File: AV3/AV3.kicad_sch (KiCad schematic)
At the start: 2 parts, among them U1 LCD-16X2

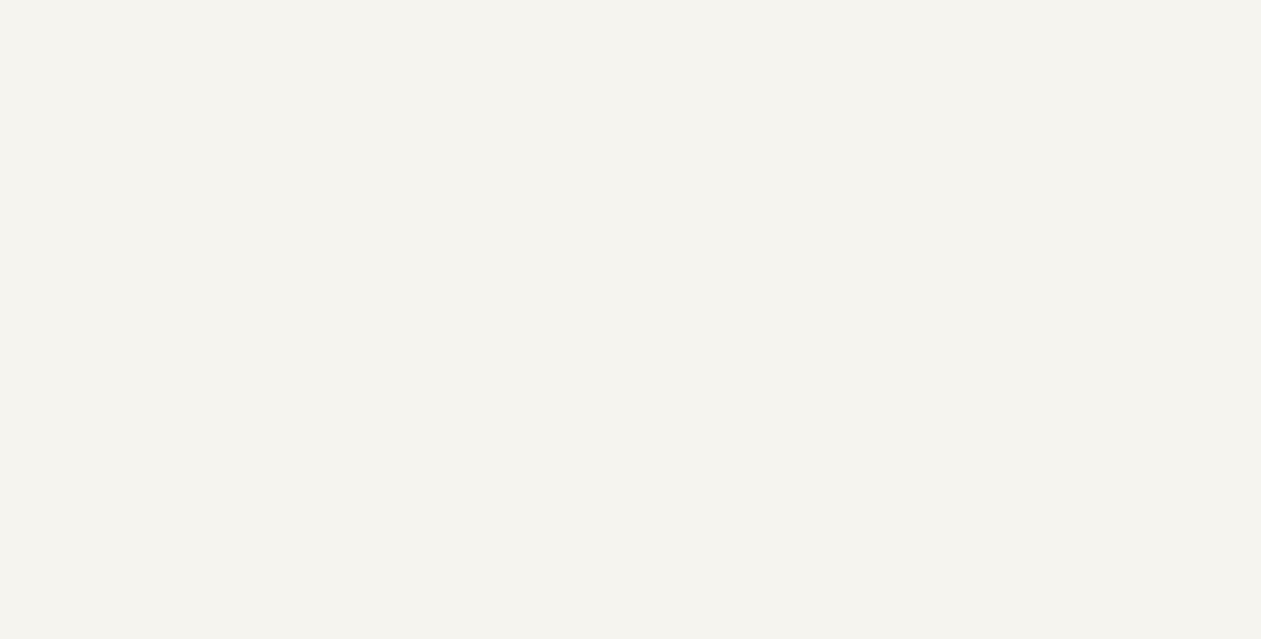
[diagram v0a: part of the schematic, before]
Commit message: Add power supply circuitry
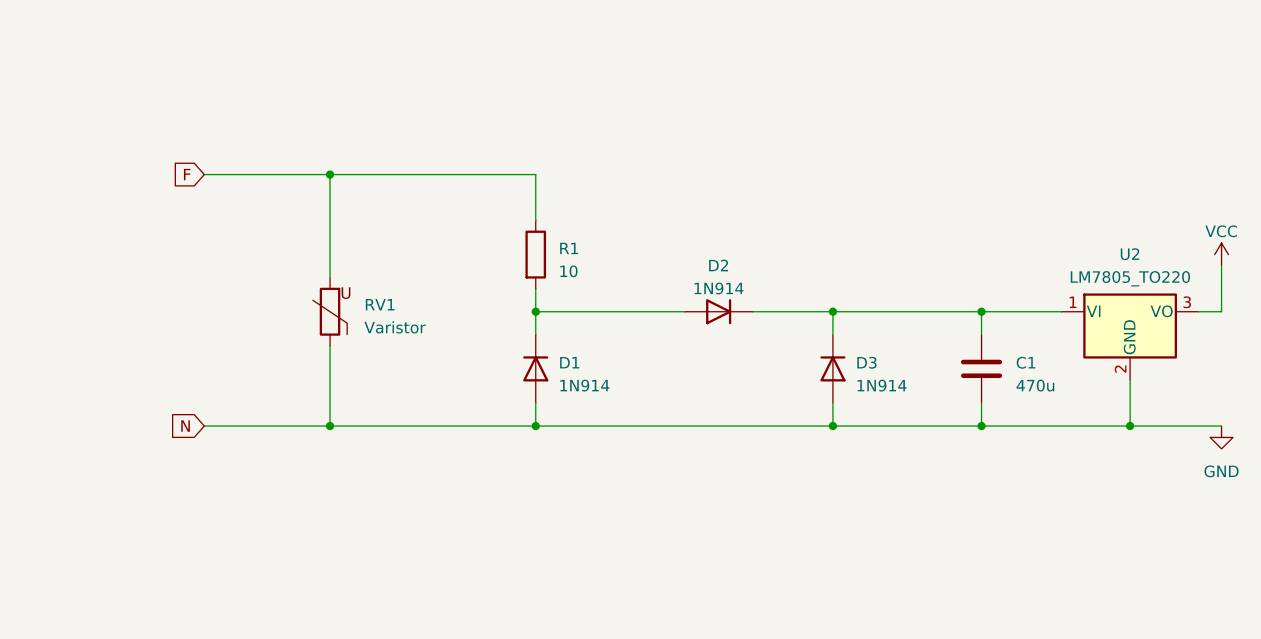
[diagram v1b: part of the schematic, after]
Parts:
- added C1: 470u, Capacitor_THT:CP_Radial_D10.0mm_P2.50mm, symbol Device:C
- added D1, D2, D3: 1N914, Diode_THT:D_DO-35_SOD27_P7.62mm_Horizontal, symbol Diode:1N914
- added R1: 10, Resistor_THT:R_Axial_DIN0204_L3.6mm_D1.6mm_P2.54mm_Vertical, symbol Device:R
- added RV1: Varistor, Varistor:RV_Disc_D7mm_W3.4mm_P5mm, symbol Device:Varistor
- added U2: LM7805_TO220, Package_TO_SOT_THT:TO-220-3_Vertical, symbol Regulator_Linear:LM7805_TO220
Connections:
- net GND: now also C1.2, D1.2 (A), D3.2 (A), RV1.1, U2.2 (GND)
- net VCC: now also U2.3 (VO)
- new net: C1.1, D2.1 (K), D3.1 (K), U2.1 (VI)
- new net: D1.1 (K), D2.2 (A), R1.2
- new net F: R1.1, RV1.2

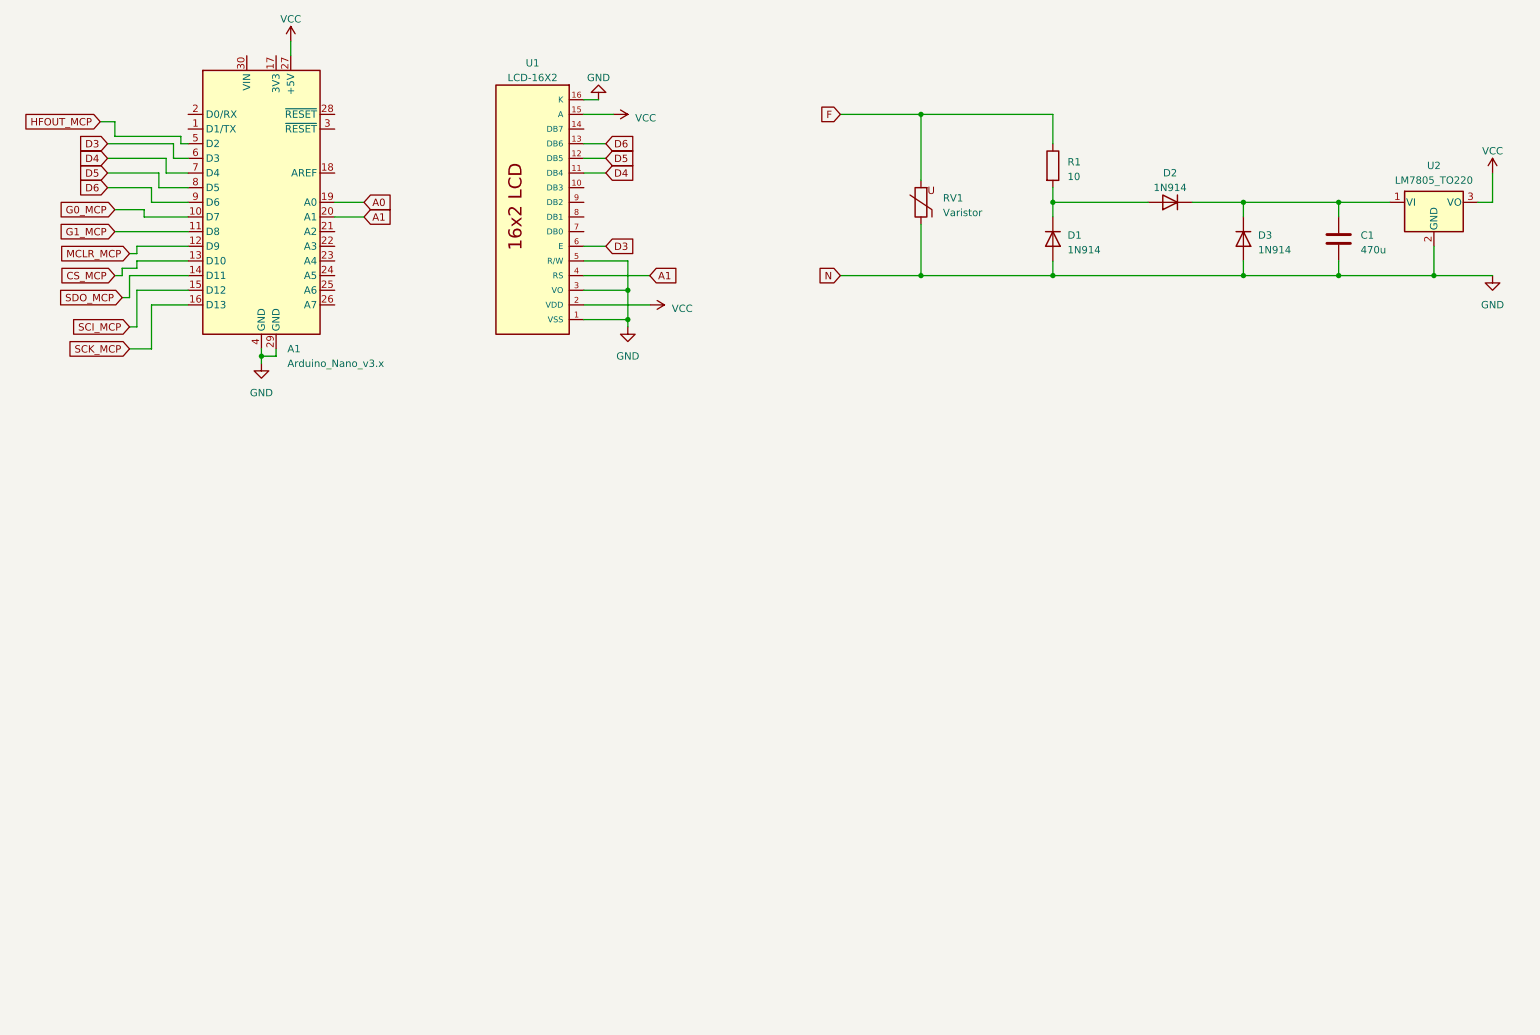
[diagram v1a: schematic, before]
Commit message: Add MCP3909
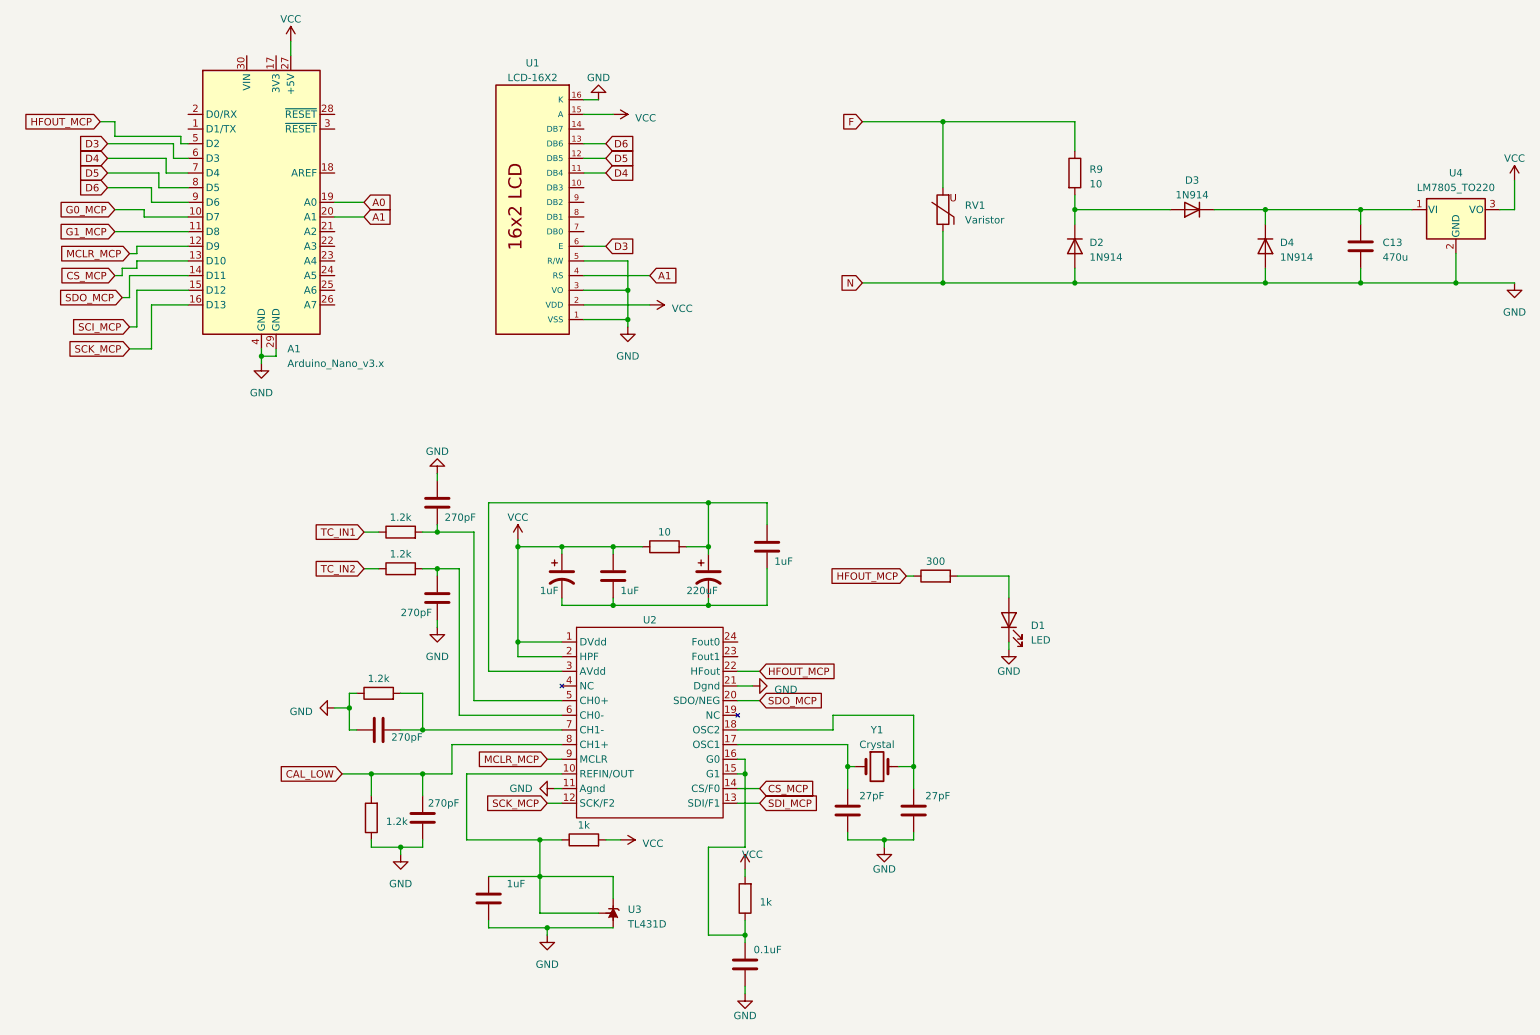
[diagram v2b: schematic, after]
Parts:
- removed D1: 1N914, Diode_THT:D_DO-35_SOD27_P7.62mm_Horizontal, symbol Diode:1N914
- removed U2: LM7805_TO220, Package_TO_SOT_THT:TO-220-3_Vertical, symbol Regulator_Linear:LM7805_TO220
- added C10: 0.1uF, Capacitor_THT:CP_Radial_D10.0mm_P2.50mm, symbol Device:C
- added C11, C12: 27pF, Capacitor_THT:CP_Radial_D10.0mm_P2.50mm, symbol Device:C
- added C13: 470u, Capacitor_THT:CP_Radial_D10.0mm_P2.50mm, symbol Device:C
- added C2: 1uF, Capacitor_THT:CP_Radial_D10.0mm_P2.50mm, symbol Device:C_Polarized_US
- added C3: 220uF, Capacitor_THT:CP_Radial_D10.0mm_P2.50mm, symbol Device:C_Polarized_US
- added C4, C9: 1uF, Capacitor_THT:CP_Radial_D10.0mm_P2.50mm, symbol Device:C
- added C5, C6, C7, C8: 270pF, Capacitor_THT:CP_Radial_D10.0mm_P2.50mm, symbol Device:C
- added D1: LED, symbol Device:LED
- added D4: 1N914, Diode_THT:D_DO-35_SOD27_P7.62mm_Horizontal, symbol Diode:1N914
- added R2, R3, R4, R5: 1.2k, Resistor_THT:R_Axial_DIN0204_L3.6mm_D1.6mm_P2.54mm_Vertical, symbol Device:R
- added R6, R7: 1k, Resistor_THT:R_Axial_DIN0204_L3.6mm_D1.6mm_P2.54mm_Vertical, symbol Device:R
- added R8: 300, Resistor_THT:R_Axial_DIN0204_L3.6mm_D1.6mm_P2.54mm_Vertical, symbol Device:R
- added R9: 10, Resistor_THT:R_Axial_DIN0204_L3.6mm_D1.6mm_P2.54mm_Vertical, symbol Device:R
- added U2: ~, MCP3909-I/SS:SOP65P780X200-24N, symbol Power_Management:MCP3909-I/SS
- added U3: TL431D, Package_SO:SOIC-8_3.9x4.9mm_P1.27mm, symbol Reference_Voltage:TL431D
- added U4: LM7805_TO220, Package_TO_SOT_THT:TO-220-3_Vertical, symbol Regulator_Linear:LM7805_TO220
- added Y1: Crystal, symbol Device:Crystal
- C1: value 470u -> 1uF
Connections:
- net CS_MCP: now also U2.14 (CS/F0)
- net F: now also R9.1; no longer R1.1
- net GND: now also D2.2 (A), C10.1, C11.1, C12.1, C13.2, C5.1, C6.2, C7.1, C8.1, C9.1, D1.1 (K), D4.2 (A), R4.1, R5.1, U2.11 (Agnd), U2.21 (Dgnd), U3.2 (A), U3.3 (A), U3.6 (A), U3.7 (A), U4.2 (GND); no longer C1.2, D3.2 (A)
- net HFOUT_MCP: now also R8.1, U2.22 (HFout)
- net MCLR_MCP: now also U2.9 (MCLR)
- net SCK_MCP: now also U2.12 (SCK/F2)
- net SDO_MCP: now also U2.20 (SDO/NEG)
- net VCC: now also C1.1, R1.1, C2.1, R6.2, R7.2, U2.1 (DVdd), U2.2 (HPF), U4.3 (VO)
- net at R1.2: now also C3.1, C4.1, U2.3 (AVdd); no longer D2.2 (A)
- new net: C13.1, D3.1 (K), D4.1 (K), U4.1 (VI)
- new net: D2.1 (K), D3.2 (A), R9.2
- new net: C12.2, U2.18 (OSC2), Y1.2
- new net: C9.2, R6.1, U2.10 (REFIN/OUT), U3.1 (K), U3.8 (REF)
- new net: C10.2, R7.1, U2.15 (G1), U2.16 (G0)
- new net: C11.2, U2.17 (OSC1), Y1.1
- new net: C5.2, R2.2, U2.5 (CH0+)
- new net: C6.1, R3.2, U2.6 (CH0-)
- new net: C7.2, R4.2, U2.7 (CH1-)
- new net: C1.2, C2.2, C3.2, C4.2
- new net: D1.2 (A), R8.2
- new net CAL_LOW: C8.2, R5.2, U2.8 (CH1+)
- new net SDI_MCP: U2.13 (SDI/F1)
- new net TC_IN1: R2.1
- new net TC_IN2: R3.1

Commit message: footprint mcp3909
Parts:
- D1: footprint (none) -> LED_THT:LED_D3.0mm
- U1: footprint (none) -> Display:LCD-016N002L
- Y1: footprint (none) -> Crystal:Crystal_HC52-6mm_Vertical
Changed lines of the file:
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@@
       (effects (font (size 1.27 1.27)))
     )
-    (property "Footprint" "" (at 101.6 54.61 0)
+    (property "Footprint" "Display:LCD-016N002L" (at 101.6 54.61 0)
       (effects (font (size 1.27 1.27)) hide)
     )
@@
       (effects (font (size 1.27 1.27)))
     )
-    (property "Footprint" "" (at 162.56 152.4 0)
+    (property "Footprint" "Crystal:Crystal_HC52-6mm_Vertical" (at 162.56 152.4 0)
       (effects (font (size 1.27 1.27)) hide)
     )
@@
       (effects (font (size 1.27 1.27)) (justify right))
     )
-    (property "Footprint" "" (at 185.42 127 0)
-      (effects (font (size 1.27 1.27)) hide)
-    )
+    (property "Footprint" "LED_THT:LED_D3.0mm" (at 185.42 127 0)
+      (effects (font (size 1.27 1.27)) hide)
+    )
